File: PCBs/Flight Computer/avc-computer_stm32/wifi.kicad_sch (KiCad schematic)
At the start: 1 part, among them J7 Conn_02x04_Odd_Even

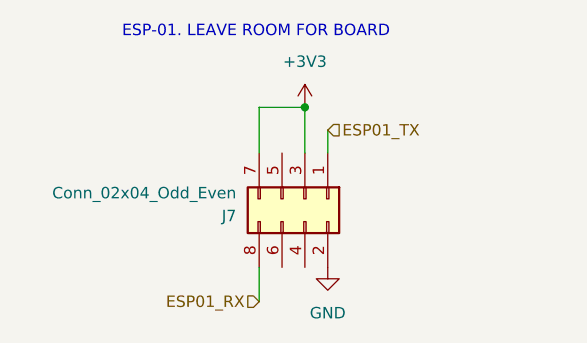
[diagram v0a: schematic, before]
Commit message: Began fixing reference designators
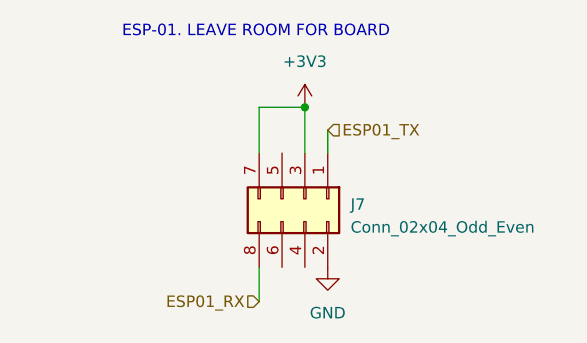
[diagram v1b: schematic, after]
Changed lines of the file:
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@@
   (symbol (lib_id "power:GND") (at 139.7 73.66 0) (mirror y) (unit 1)
     (in_bom yes) (on_board yes) (dnp no) (fields_autoplaced)
-    (property "Reference" "#PWR02" (at 139.7 80.01 0)
+    (property "Reference" "#PWR049" (at 139.7 80.01 0)
       (effects (font (size 1.27 1.27)) hide)
     )
@@
       (project "avc-computer"
         (path "/e63e39d7-6ac0-4ffd-8aa3-1841a4541b55/144aa036-8f15-4412-804a-63168122b29e"
-          (reference "#PWR02") (unit 1)
+          (reference "#PWR049") (unit 1)
         )
       )
@@
   (symbol (lib_id "Connector_Generic:Conn_02x04_Odd_Even") (at 137.16 66.04 270) (unit 1)
     (in_bom yes) (on_board yes) (dnp no) (fields_autoplaced)
-    (property "Reference" "J7" (at 129.54 67.945 90)
-      (effects (font (size 1.27 1.27)) (justify right))
+    (property "Reference" "J7" (at 142.24 66.675 90)
+      (effects (font (size 1.27 1.27)) (justify left))
     )
-    (property "Value" "Conn_02x04_Odd_Even" (at 129.54 65.405 90)
-      (effects (font (size 1.27 1.27)) (justify right))
+    (property "Value" "Conn_02x04_Odd_Even" (at 142.24 69.215 90)
+      (effects (font (size 1.27 1.27)) (justify left))
     )
     (property "Footprint" "Connector_PinHeader_2.54mm:PinHeader_2x04_P2.54mm_Vertical" (at 137.16 66.04 0)
@@
   (symbol (lib_id "power:+3V3") (at 137.16 55.88 0) (mirror y) (unit 1)
     (in_bom yes) (on_board yes) (dnp no) (fields_autoplaced)
-    (property "Reference" "#PWR01" (at 137.16 59.69 0)
+    (property "Reference" "#PWR048" (at 137.16 59.69 0)
       (effects (font (size 1.27 1.27)) hide)
     )
@@
       (project "avc-computer"
         (path "/e63e39d7-6ac0-4ffd-8aa3-1841a4541b55/144aa036-8f15-4412-804a-63168122b29e"
-          (reference "#PWR01") (unit 1)
+          (reference "#PWR048") (unit 1)
         )
       )
